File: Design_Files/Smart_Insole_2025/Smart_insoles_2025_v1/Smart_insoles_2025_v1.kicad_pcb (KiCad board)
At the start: 4 copper layers, 69.7 x 30.1 mm, 78 parts, among them IC1 USBLC6-2SC6, J1 Conn_01x20, J2 USB_C_Receptacle_USB2.0_16P, J4 S2B-PH-SM4-TB_LF__SN_, Q2 FDN306P, SW1 RESET, SW2 BOOT, U1 ME6211C33M5, U2 CD74HC4067M96, U3 LSM6DSO32TR, U5 ESP32-C3-MINI-1-N4, U7 BQ24040DSQR, U8 MCP6004-I_ST, U9 MCP6004-I_ST

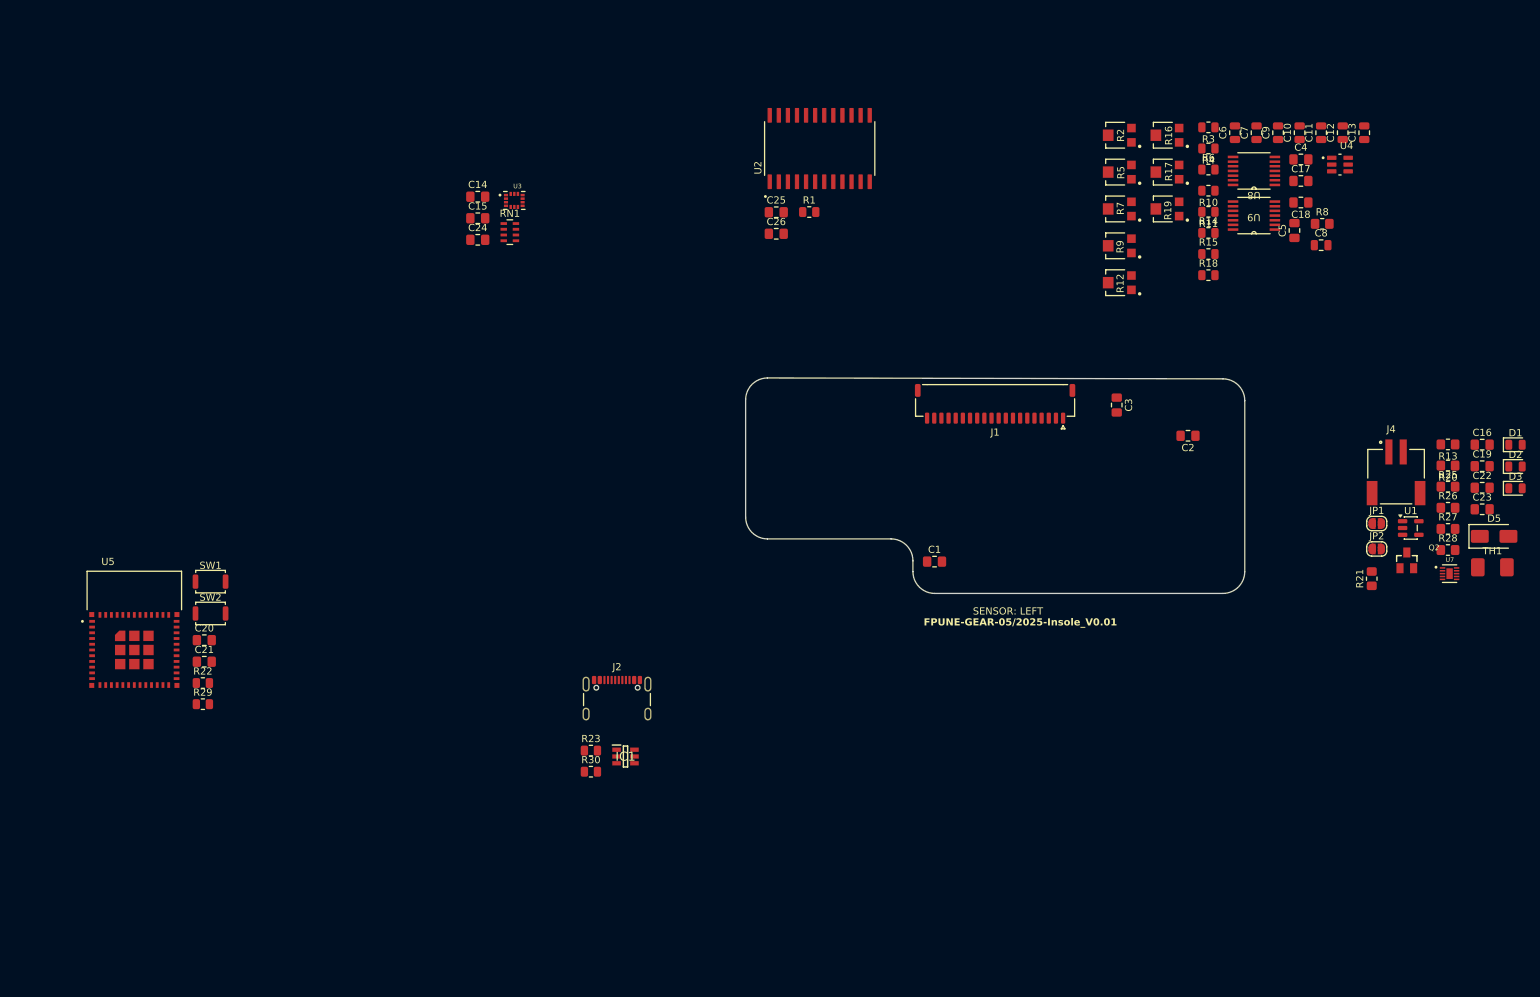
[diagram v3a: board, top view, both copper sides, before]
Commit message: SCH: Added Power Test points and Mounting Holes. PCB: Arranged grouped  Footprints to minimize rounting
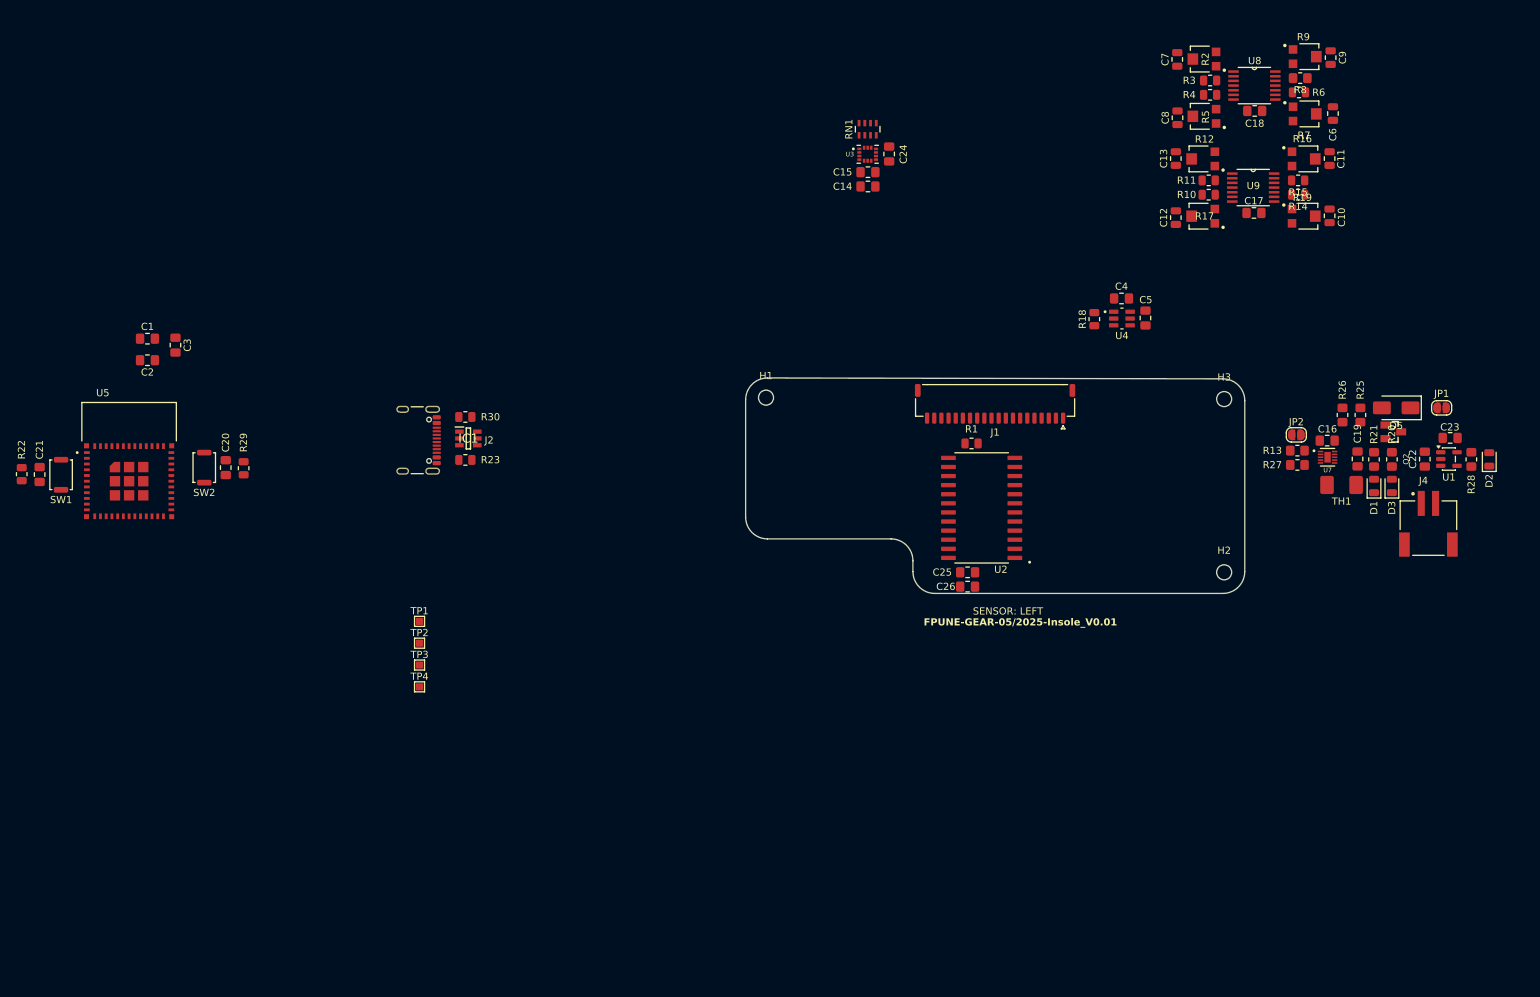
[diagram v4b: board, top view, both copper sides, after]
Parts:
- added H1: MountingHole, MountingHole:MountingHole_2.1mm, F.Cu at (76.0, 21.8)
- added H2: MountingHole, MountingHole:MountingHole_2.1mm, F.Cu at (140.0, 46.2)
- added H3: MountingHole, MountingHole:MountingHole_2.1mm, F.Cu at (140.0, 22.0)
- added TP1: TestPoint_Alt, TestPoint:TestPoint_Pad_1.0x1.0mm, F.Cu at (27.6, 53.0)
- added TP2: TestPoint_Alt, TestPoint:TestPoint_Pad_1.0x1.0mm, F.Cu at (27.6, 56.1)
- added TP3: TestPoint_Alt, TestPoint:TestPoint_Pad_1.0x1.0mm, F.Cu at (27.6, 59.1)
- added TP4: TestPoint_Alt, TestPoint:TestPoint_Pad_1.0x1.0mm, F.Cu at (27.6, 62.2)
- moved C2 145.7 mm to (-10.4, 16.6)
- moved C3 131.8 mm to (-6.50, 14.5)
- moved C1 114.3 mm to (-10.4, 13.6)
- moved C24 58.7 mm to (93.2, -12.2), turned to 90 degrees
- moved C25 57.0 mm to (104.2, 46.2)
- moved C26 56.1 mm to (104.2, 48.2)
- moved U2 55.1 mm to (106.1, 37.2), turned to 180 degrees
- moved C15 54.9 mm to (90.2, -9.70)
- moved C14 54.5 mm to (90.2, -7.70)
- moved R30 52.6 mm to (34.0, 24.5)
- moved RN1 52.0 mm to (90.2, -15.7), turned to 90 degrees
- moved U3 49.8 mm to (90.2, -12.2)
- moved IC1 49.6 mm to (34.4, 27.5)
- moved J2 47.1 mm to (26.3, 27.8), turned to -90 degrees
- moved R23 44.2 mm to (34.0, 30.5)
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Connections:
- net /Battery Circuit Options/Vsel renamed Vsel
- net Net-(D5-A) renamed /Battery Circuit Options/IN

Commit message: SCH: Added FSR_In missing connections.
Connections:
- J1 pad 18: unconnected-(J1-Pin_18-Pad18) -> /FSR_AnalogFE/FSR_IN
- J1 pad 19: unconnected-(J1-Pin_19-Pad19) -> /FSR_AnalogFE/FSR_IN
- J1 pad 20: unconnected-(J1-Pin_20-Pad20) -> /FSR_AnalogFE/FSR_IN

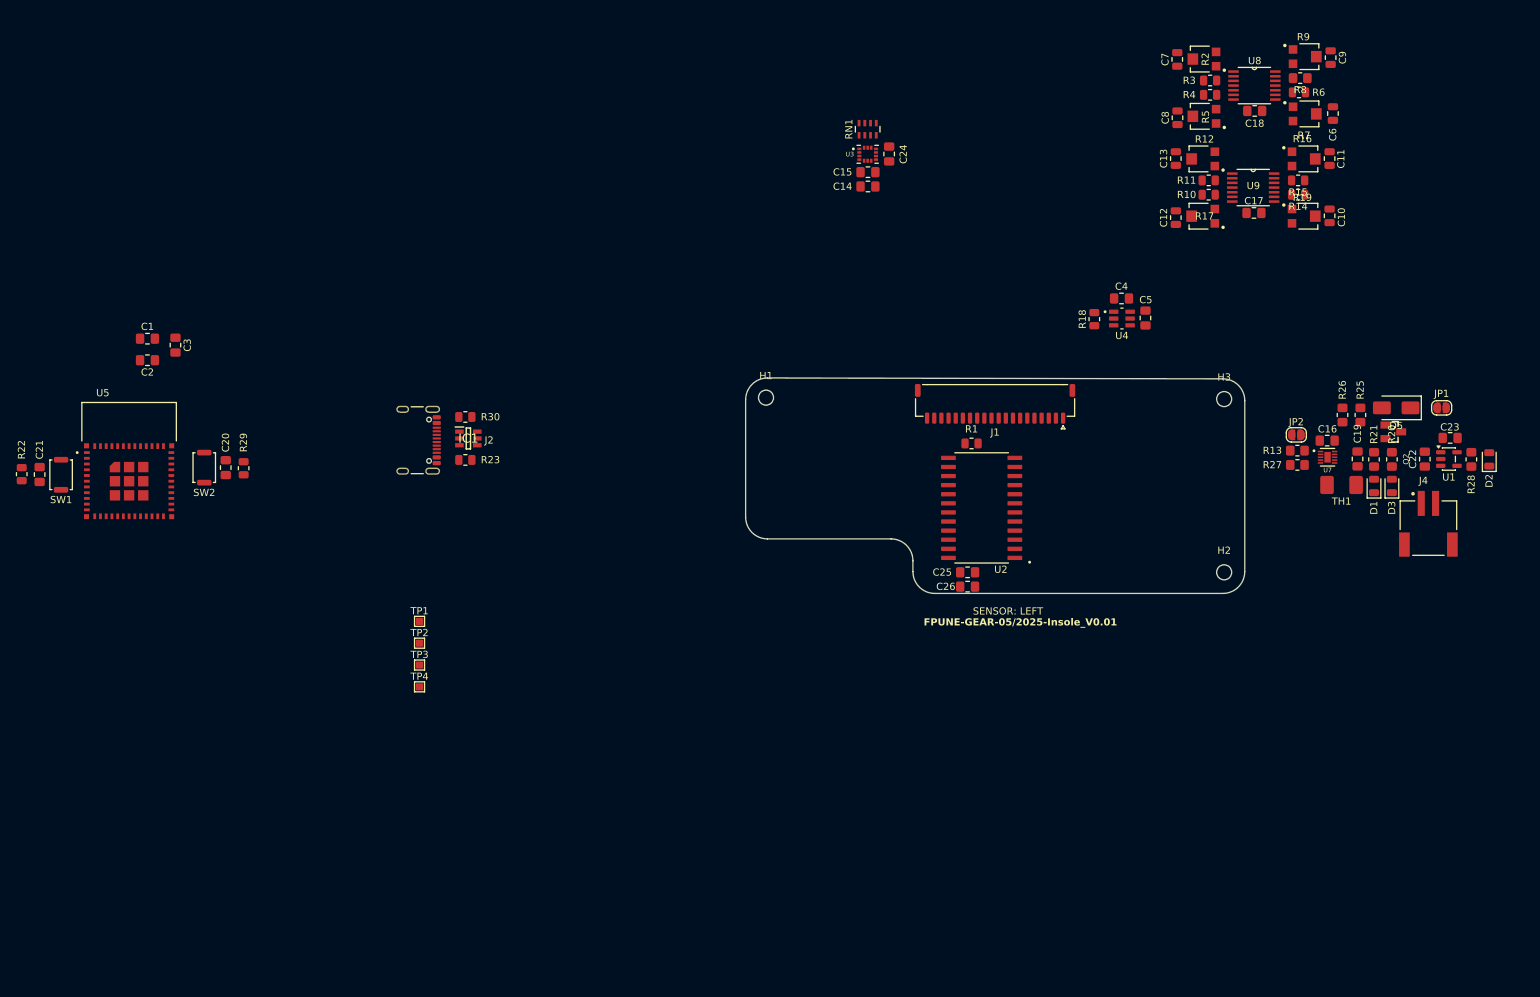
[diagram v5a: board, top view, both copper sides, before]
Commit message: PCB:Initial positioning of grouped footprints
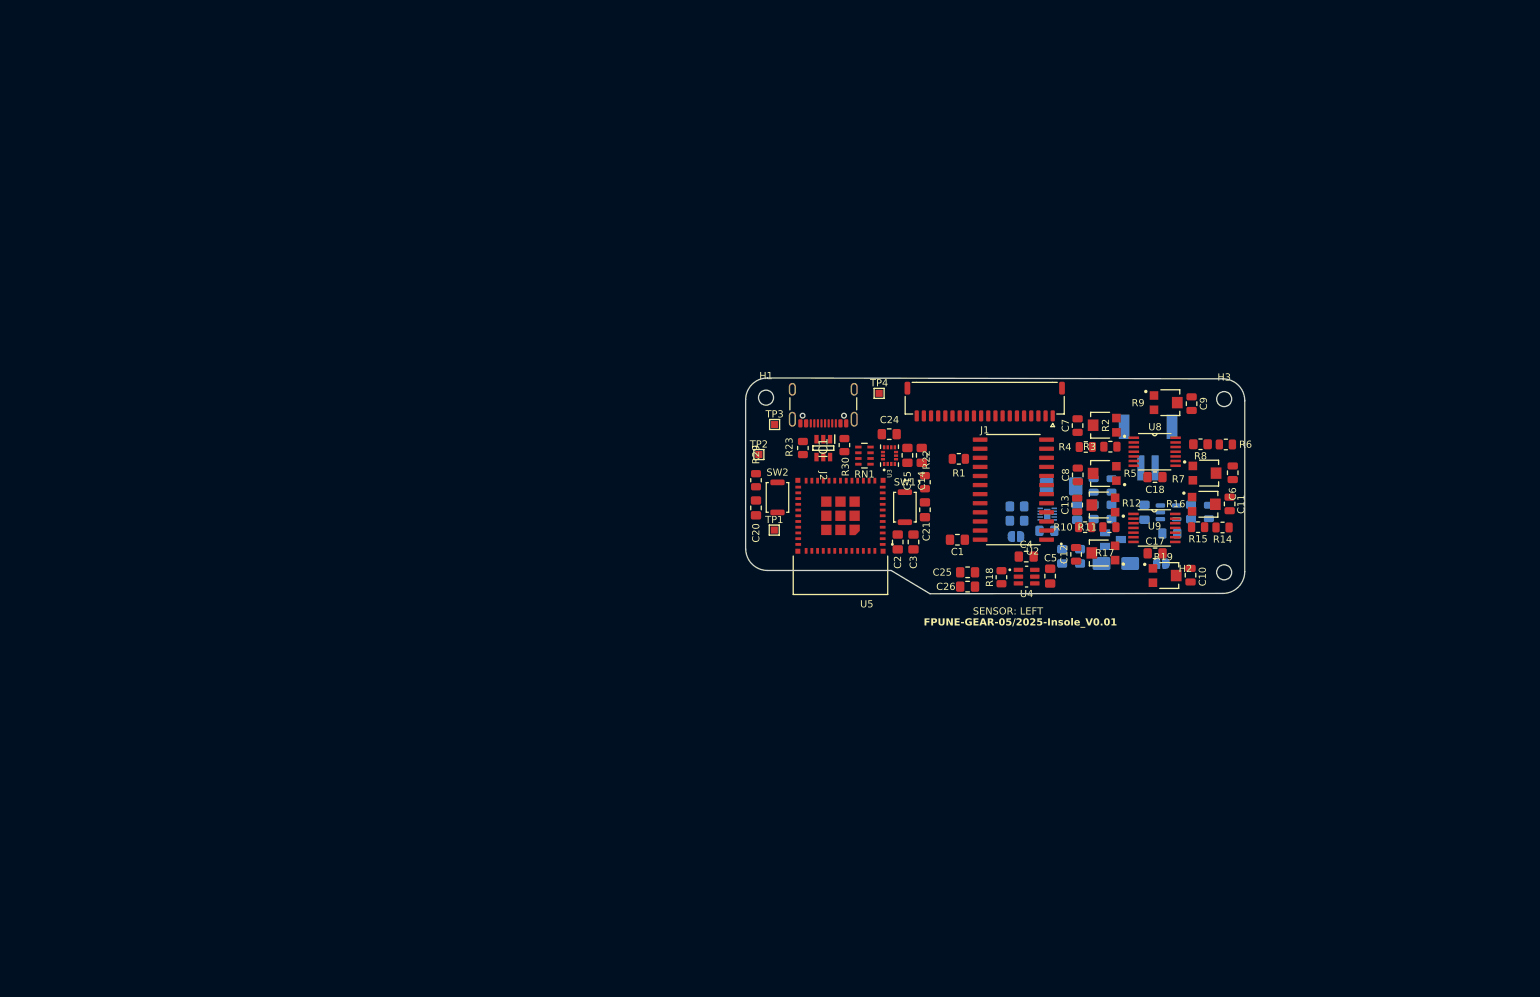
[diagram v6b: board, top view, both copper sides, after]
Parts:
- C16, C19, C22, C23, D1, D2, D3, D5, J4, JP1, JP2, Q2, R13, R20, R21, R25, R26, R27, R28, TH1, U1, U7: moved to B.Cu
- moved R22 126.2 mm to (98.2, 33.6)
- moved C21 123.8 mm to (98.2, 37.5), turned to 90 degrees
- moved SW1 118.0 mm to (95.4, 37.1), turned to 90 degrees
- moved C1 116.6 mm to (102.7, 41.6), turned to 180 degrees
- moved C2 107.8 mm to (94.4, 42.0), turned to -90 degrees
- moved C3 106.7 mm to (96.6, 42.0), turned to 90 degrees
- moved U5 99.9 mm to (86.4, 41.0), turned to 180 degrees
- moved SW2 80.2 mm to (77.6, 35.7), turned to 90 degrees
- moved TP4 76.2 mm to (91.8, 21.2)
- moved C20 74.3 mm to (74.6, 37.2), turned to 90 degrees
- moved R29 71.6 mm to (74.6, 33.3)
- moved TP3 59.9 mm to (77.2, 25.6)
- moved J2 58.0 mm to (84.0, 21.7), turned to 180 degrees
- moved TP2 54.2 mm to (75.0, 29.8)
- moved R19 53.8 mm to (131.8, 46.6)
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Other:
- outline, holes or cut-outs redrawn

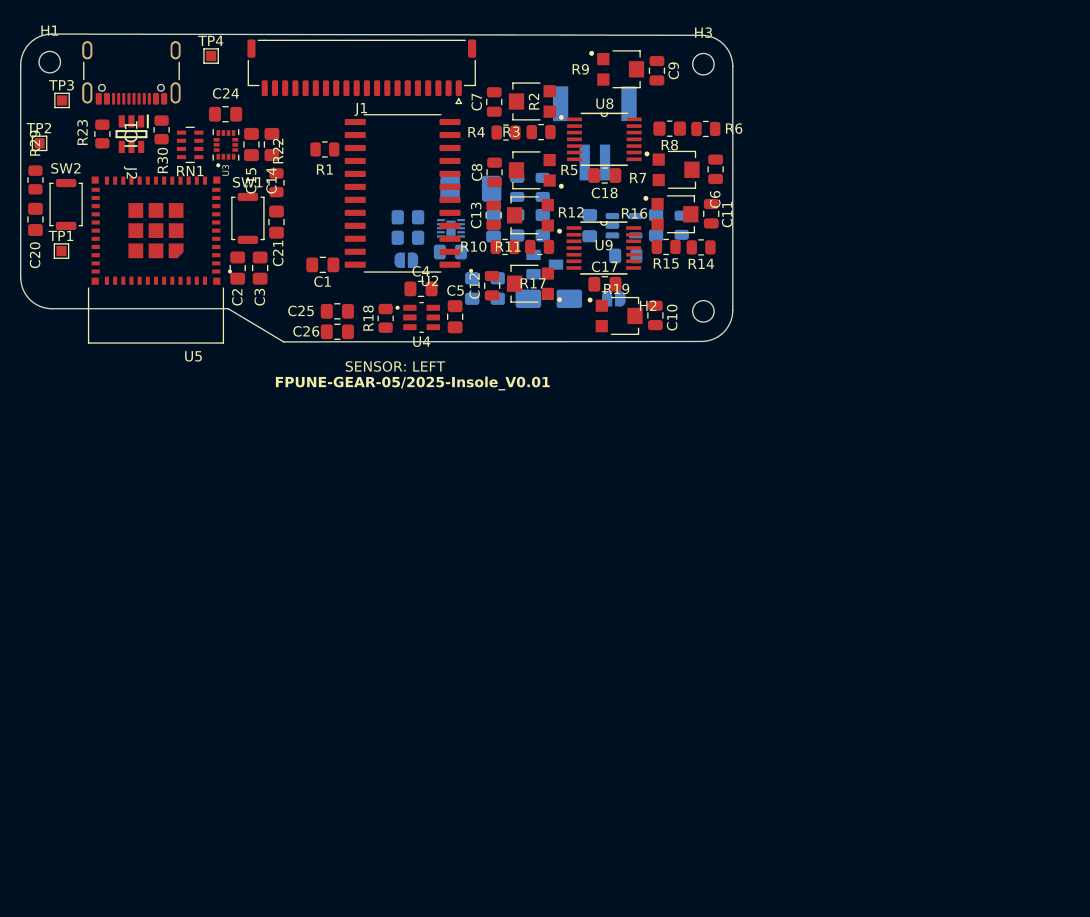
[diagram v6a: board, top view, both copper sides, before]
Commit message: PCB: Added 3d models to all components. Also preliminar routing of componentes. Component placemente needs checking.
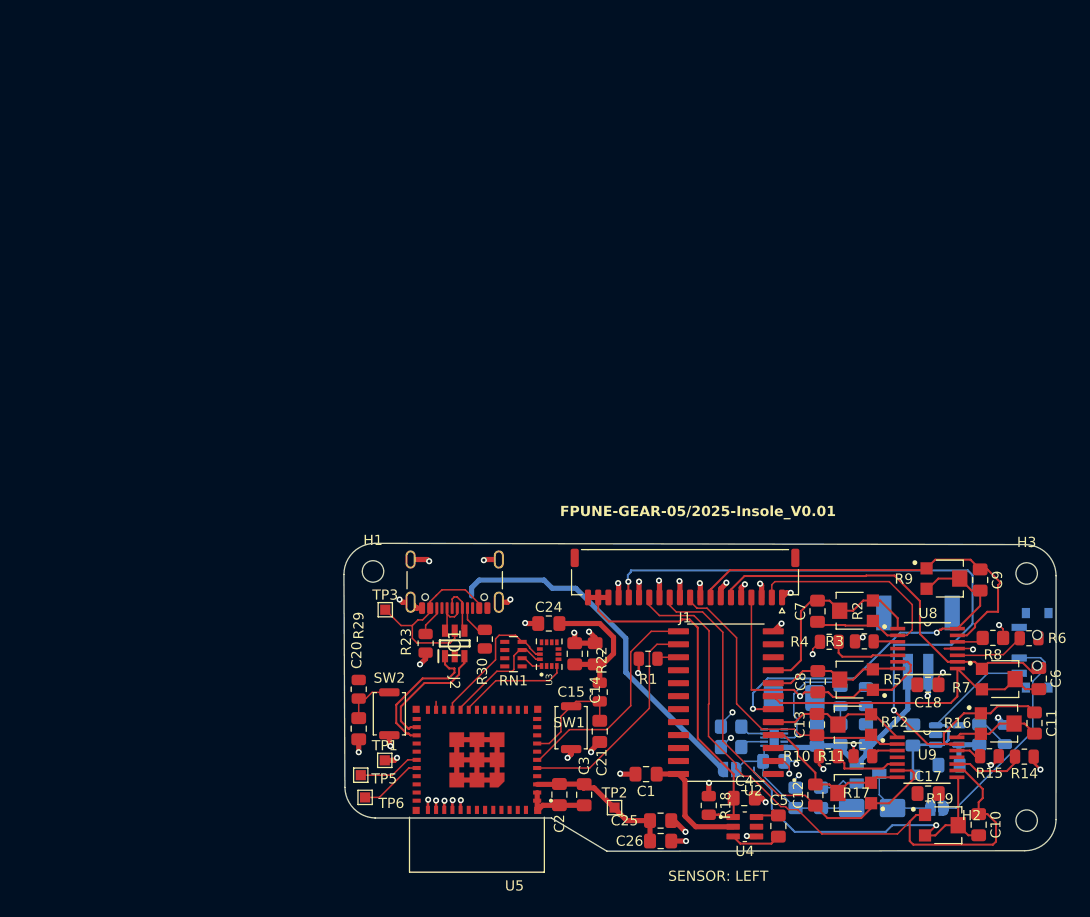
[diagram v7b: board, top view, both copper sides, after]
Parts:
- added SW3: SW_Nidec_CAS-120A1, Button_Switch_SMD:SW_SPDT_PCM12, B.Cu at (172.4, 79.4)
- added TP5: TestPoint_Alt, TestPoint:TestPoint_Pad_1.0x1.0mm, F.Cu at (106.5, 91.6)
- added TP6: TestPoint_Alt, TestPoint:TestPoint_Pad_1.0x1.0mm, F.Cu at (106.9, 93.8)
- C10, C11, C12, C13, C6, C7, C8, C9: footprint Capacitor_SMD:C_0805_2012Metric -> Capacitor_SMD:C_0805_2012Metric_Pad1.18x1.45mm_HandSolder
- TP4: moved to B.Cu
- moved TP4 98.5 mm to (160.7, 91.6), turned to 180 degrees
- moved TP2 86.0 mm to (131.3, 94.8)
- moved U5 60.6 mm to (117.8, 92.8)
- moved C3 60.5 mm to (128.3, 93.5), turned to -90 degrees
- moved C2 60.4 mm to (125.9, 93.5)
- moved C12 59.1 mm to (151.0, 93.6)
- moved C14 59.1 mm to (129.4, 79.7)
- moved C15 59.1 mm to (127.4, 79.7)
- moved D5 59.1 mm to (156.5, 94.8)
- moved H1 59.1 mm to (107.7, 71.7)
- moved R13 59.1 mm to (142.7, 88.9)
- moved R14 59.1 mm to (171.4, 89.8)
- moved R2 59.1 mm to (154.8, 75.5)
- moved R22 59.1 mm to (129.8, 83.5)
- moved R25 59.1 mm to (151.5, 93.8)
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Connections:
- JP1 pad 2: Vsel -> Net-(JP1-B)
- U3 pad 2: unconnected-(U3-SDX-Pad2) -> SDX
- U3 pad 3: unconnected-(U3-SCX-Pad3) -> SCX
- U3 pad 9: unconnected-(U3-INT2-Pad9) -> INT2
- U5 pad 16: unconnected-(U5-IO10-Pad16) -> IO10
- U5 pad 22: unconnected-(U5-IO8-Pad22) -> IO8
- U5 pad 30: unconnected-(U5-RXD0-Pad30) -> RX
- U5 pad 31: unconnected-(U5-TXD0-Pad31) -> TX
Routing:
- net GND: track 0.00 -> 104.1 mm, vias 0 -> 50
- net /FSR_AnalogFE/FSR_OUT_7: track 0.00 -> 76.2 mm, vias 0 -> 2
- net /FSR_AnalogFE/FSR_OUT_6: track 0.00 -> 64.6 mm
- net VBUS: track 0.00 -> 54.8 mm
- net +3V3: track 0.00 -> 45.1 mm
- net /FSR_AnalogFE/FSR_OUT_5: track 0.00 -> 43.7 mm
- net /FSR_AnalogFE/FSR_OUT_3: track 0.00 -> 39.4 mm
- net /FSR_AnalogFE/FSR_OUT_2: track 0.00 -> 37.3 mm
- net I3: track 0.00 -> 37.0 mm, vias 0 -> 2
- net /FSR_AnalogFE/FSR_IN: track 0.00 -> 36.4 mm
- net I6: track 0.00 -> 34.4 mm, vias 0 -> 1
- net I2: track 0.00 -> 30.9 mm
- net /FSR_AnalogFE/FSR_OUT_4: track 0.00 -> 30.5 mm
- net /FSR_AnalogFE/FSR_OUT_0: track 0.00 -> 29.0 mm
- net /FSR_AnalogFE/FSR_OUT_1: track 0.00 -> 28.3 mm, vias 0 -> 1
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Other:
- outline, holes or cut-outs redrawn
